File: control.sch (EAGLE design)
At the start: 21 parts, among them IC1 OPA336P, Q1 BSS92, Q2 BSS101

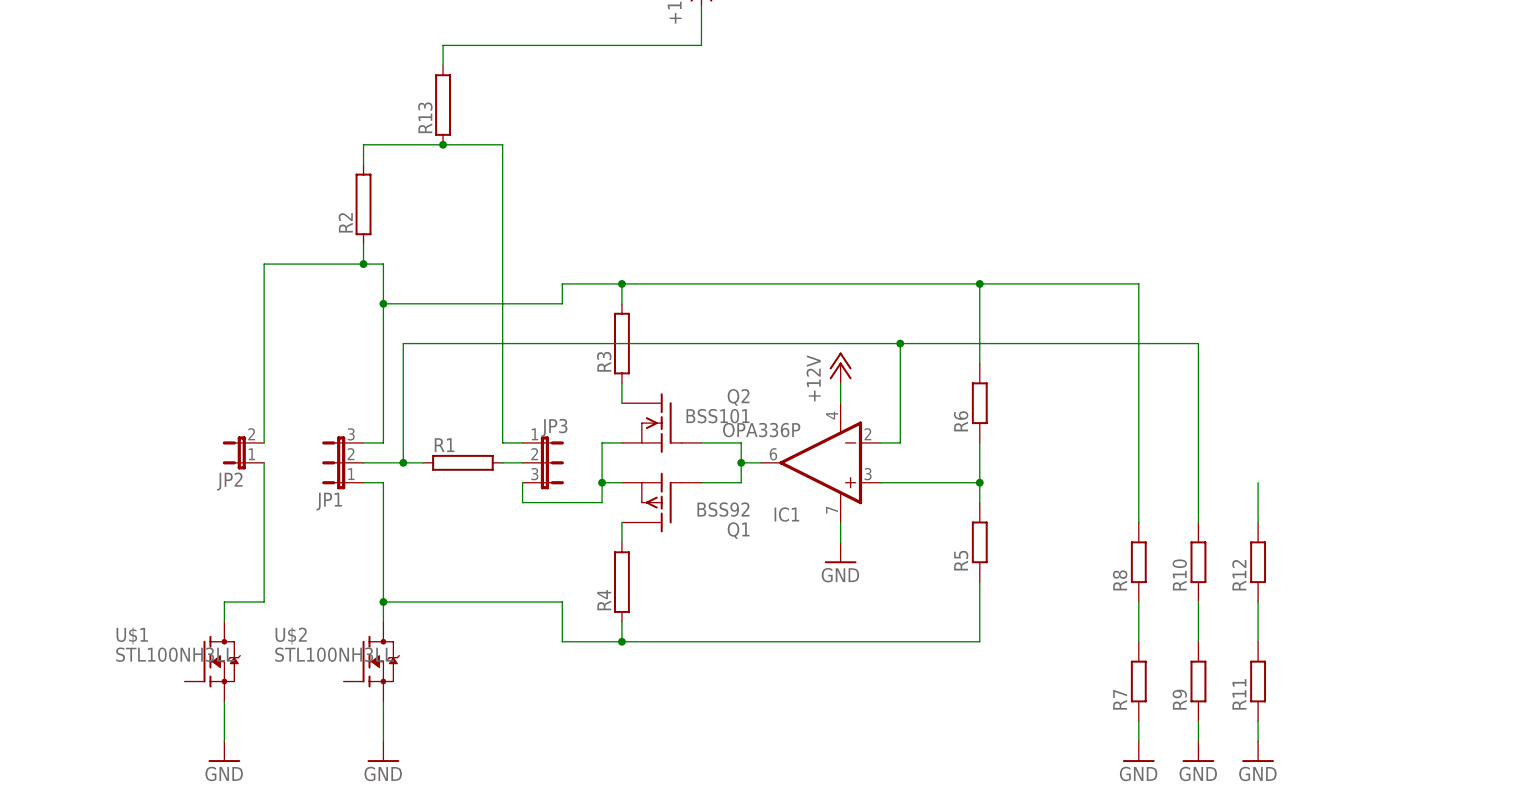
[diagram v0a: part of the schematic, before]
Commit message: +added main discharge path
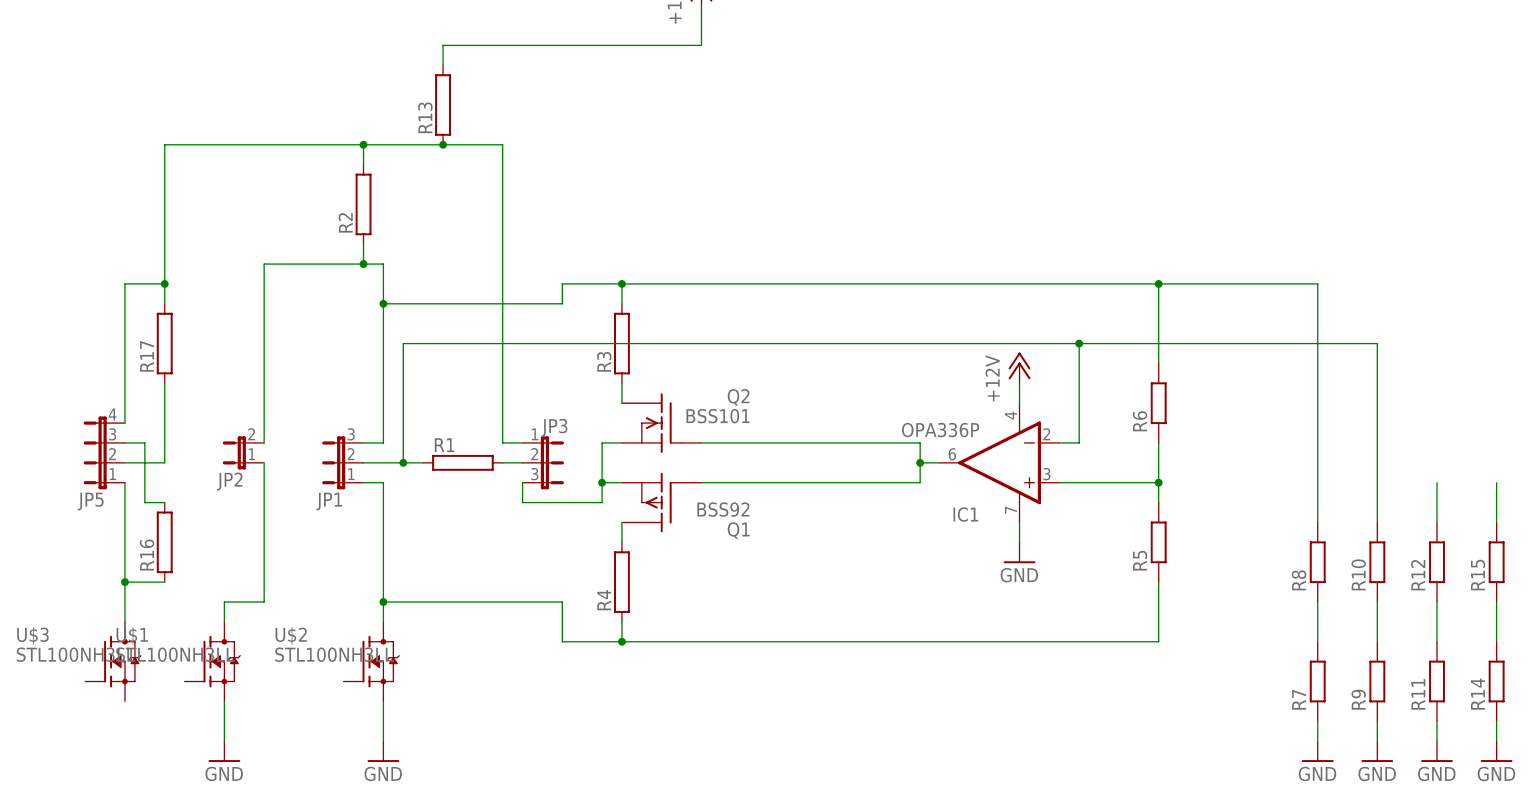
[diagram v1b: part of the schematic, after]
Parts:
- added JP5: (no value), jumper:JP4E
- added R14, R15: (no value), resistor:R-EU_M0805
- added R16, R17: (no value), resistor-power:RRS02M
- added U$3: STL100NH3LL, teile:STL100NH3LL
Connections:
- new net ADC4: JP3.1, JP5.4, R13.1, R15.2, R17.2, R2.2
- new net N$14: JP5.1, R16.1, U$3.D
- new net N$15: JP5.3, R16.2
- new net N$16: JP5.2, R17.1
- net GND: now also R14.1
- net N$10: now also R14.2, R15.1; no longer JP3.1, R13.1, R2.2
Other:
- moved on the sheet: IC1, R10, R11, R12, R5, R6, R7, R8, R9

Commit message: +µC
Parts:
- removed R13: (no value), resistor-power:RRWM5X26
- added C1, C2, C3, C4, C5, C6: (no value), resistor:C-EUC0805K
- added IC2: XMEGA16A4A, atmel:XMEGA16A4A
- added IC3: LM317MBSTT3, v-reg:LM317MBSTT3
- added JP4, JP6: (no value), jumper:JP4E
- added R18, R19, R20: (no value), resistor:R-EU_M0805
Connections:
- new net +3V3: C1.1, C2.1, C3.1, C4.1, C5.1, IC2.AVCC, IC2.VCC, IC2.VCC1, IC2.VCC2, IC3.OUT, R18.2, R20.2
- new net N$17: IC2.!RESET!/PDI_CLK, R18.1
- new net N$18: IC2.PA0, JP6.4
- new net N$19: IC2.PA1, JP6.3
- new net N$20: IC2.PA2, JP6.2
- new net N$21: IC2.PA3, JP6.1
- new net N$22: IC2.PA4, JP4.4
- new net N$23: IC2.PA5, JP4.3
- new net N$24: IC2.PA6, JP4.2
- new net N$25: IC2.PA7, JP4.1
- new net N$27: IC3.ADJ, R19.2, R20.1
- net +12V: now also C6.1, IC3.IN; no longer R13.2
- net ADC4: no longer R13.1
- net GND: now also C1.2, C2.2, C3.2, C4.2, C5.2, C6.2, IC2.GND, IC2.GND1, IC2.GND2, IC2.GND3, R19.1

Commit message: +spannungsregler
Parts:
- added C7, C8: (no value), resistor:C-EUC0805K
- added IC4: OPA336P, burr-brown:OPA336P
- added Q5: TIP41C, transistor-power:TIP41C
- added Q6: TIP42C, transistor-power:TIP42C
- added Q7: BC338, transistor-npn:BC338
- added R13, R21, R22: (no value), resistor:R-EU_M0805
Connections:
- new net N$12: C7.1, Q5.E, R22.1
- new net N$13: Q7.C, R13.2
- new net N$26: Q6.B, R13.1
- new net N$28: C8.1, IC4.OUT, Q7.B
- new net N$30: C8.2, IC4.-IN, R21.1, R22.2
- new net N$31: IC2.PB0, IC4.+IN
- new net N$32: Q5.B, Q6.C
- net +12V: now also IC4.V-, Q5.C, Q6.E
- net GND: now also C7.2, IC4.V+, Q7.E, R21.2
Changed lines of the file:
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@@
 <part name="JP4" library="jumper" deviceset="JP4E" device=""/>
 <part name="JP6" library="jumper" deviceset="JP4E" device=""/>
+<part name="R13" library="resistor" deviceset="R-EU_" device="M0805"/>
+<part name="IC4" library="burr-brown" deviceset="OPA336" device="P"/>
+<part name="R21" library="resistor" deviceset="R-EU_" device="M0805"/>
+<part name="R22" library="resistor" deviceset="R-EU_" device="M0805"/>
+<part name="C7" library="resistor" deviceset="C-EU" device="C0805K"/>
+<part name="C8" library="resistor" deviceset="C-EU" device="C0805K"/>
+<part name="GND13" library="supply1" deviceset="GND" device=""/>
+<part name="GND14" library="supply1" deviceset="GND" device=""/>
+<part name="GND15" library="supply1" deviceset="GND" device=""/>
+<part name="GND16" library="supply1" deviceset="GND" device=""/>
+<part name="Q5" library="transistor-power" deviceset="TIP41C" device=""/>
+<part name="Q6" library="transistor-power" deviceset="TIP42C" device=""/>
+<part name="Q7" library="transistor-npn" deviceset="BC338*" device=""/>
 </parts>
 <sheets>
@@
 <instance part="GND2" gate="1" x="33.02" y="15.24"/>
 <instance part="GND3" gate="1" x="114.3" y="40.64"/>
-<instance part="P+1" gate="1" x="73.66" y="114.3"/>
+<instance part="P+1" gate="1" x="-7.62" y="165.1"/>
 <instance part="P+2" gate="1" x="114.3" y="66.04"/>
 <instance part="R7" gate="G$1" x="152.4" y="25.4" rot="R90"/>
@@
 <instance part="JP4" gate="G$1" x="170.18" y="233.68" rot="R270"/>
 <instance part="JP6" gate="G$1" x="170.18" y="223.52" rot="R270"/>
+<instance part="R13" gate="G$1" x="7.62" y="137.16" rot="R270"/>
+<instance part="IC4" gate="G$1" x="25.4" y="121.92" rot="R180"/>
+<instance part="R21" gate="G$1" x="45.72" y="119.38" rot="R270"/>
+<instance part="R22" gate="G$1" x="45.72" y="134.62" rot="R270"/>
+<instance part="C7" gate="G$1" x="63.5" y="129.54"/>
+<instance part="C8" gate="G$1" x="25.4" y="132.08" rot="R90"/>
+<instance part="GND13" gate="1" x="45.72" y="109.22"/>
+<instance part="GND14" gate="1" x="27.94" y="109.22"/>
+<instance part="GND15" gate="1" x="7.62" y="109.22"/>
+<instance part="GND16" gate="1" x="63.5" y="109.22"/>
+<instance part="Q5" gate="1" x="17.78" y="157.48" rot="R90"/>
+<instance part="Q6" gate="1" x="12.7" y="152.4" rot="R90"/>
+<instance part="Q7" gate="G$1" x="10.16" y="121.92" rot="MR0"/>
 </instances>
 <busses>
@@
 <wire x1="25.4" y1="236.22" x2="25.4" y2="243.84" width="0.1524" layer="91"/>
 </segment>
+<segment>
+<pinref part="IC4" gate="G$1" pin="V+"/>
+<pinref part="GND14" gate="1" pin="GND"/>
+<wire x1="27.94" y1="114.3" x2="27.94" y2="111.76" width="0.1524" layer="91"/>
+</segment>
+<segment>
+<pinref part="R21" gate="G$1" pin="2"/>
+<pinref part="GND13" gate="1" pin="GND"/>
+<wire x1="45.72" y1="114.3" x2="45.72" y2="111.76" width="0.1524" layer="91"/>
+</segment>
+<segment>
+<pinref part="GND16" gate="1" pin="GND"/>
+<pinref part="C7" gate="G$1" pin="2"/>
+<wire x1="63.5" y1="111.76" x2="63.5" y2="124.46" width="0.1524" layer="91"/>
+</segment>
+<segment>
+<pinref part="Q7" gate="G$1" pin="E"/>
+<pinref part="GND15" gate="1" pin="GND"/>
+<wire x1="7.62" y1="111.76" x2="7.62" y2="116.84" width="0.1524" layer="91"/>
+</segment>
 </net>
 <net name="+12V" class="0">
@@
 <pinref part="P+2" gate="1" pin="+12V"/>
 <wire x1="114.3" y1="60.96" x2="114.3" y2="63.5" width="0.1524" layer="91"/>
-</segment>
-<segment>
-<pinref part="P+1" gate="1" pin="+12V"/>
-<wire x1="73.66" y1="111.76" x2="73.66" y2="106.68" width="0.1524" layer="91"/>
-<wire x1="73.66" y1="106.68" x2="40.64" y2="106.68" width="0.1524" layer="91"/>
-<wire x1="40.64" y1="106.68" x2="40.64" y2="104.14" width="0.1524" layer="91"/>
 </segment>
 <segment>
@@
 <wire x1="25.4" y1="256.54" x2="25.4" y2="264.16" width="0.1524" layer="91"/>
 <junction x="25.4" y="256.54"/>
+</segment>
+<segment>
+<pinref part="P+1" gate="1" pin="+12V"/>
+<wire x1="-7.62" y1="160.02" x2="-7.62" y2="162.56" width="0.1524" layer="91"/>
+<wire x1="-7.62" y1="160.02" x2="-7.62" y2="129.54" width="0.1524" layer="91"/>
+<pinref part="IC4" gate="G$1" pin="V-"/>
+<wire x1="27.94" y1="129.54" x2="-7.62" y2="129.54" width="0.1524" layer="91"/>
+<pinref part="Q5" gate="1" pin="C"/>
+<wire x1="12.7" y1="160.02" x2="5.08" y2="160.02" width="0.1524" layer="91"/>
+<wire x1="5.08" y1="160.02" x2="5.08" y2="154.94" width="0.1524" layer="91"/>
+<pinref part="Q6" gate="1" pin="E"/>
+<wire x1="5.08" y1="154.94" x2="7.62" y2="154.94" width="0.1524" layer="91"/>
+<wire x1="5.08" y1="160.02" x2="-7.62" y2="160.02" width="0.1524" layer="91"/>
+<junction x="5.08" y="160.02"/>
 </segment>
 </net>
@@
 </segment>
 </net>
+<net name="N$12" class="0">
+<segment>
+<pinref part="C7" gate="G$1" pin="1"/>
+<wire x1="45.72" y1="144.78" x2="63.5" y2="144.78" width="0.1524" layer="91"/>
+<wire x1="63.5" y1="144.78" x2="63.5" y2="132.08" width="0.1524" layer="91"/>
+<pinref part="R22" gate="G$1" pin="1"/>
+<wire x1="45.72" y1="139.7" x2="45.72" y2="144.78" width="0.1524" layer="91"/>
+<pinref part="Q5" gate="1" pin="E"/>
+<wire x1="22.86" y1="160.02" x2="45.72" y2="160.02" width="0.1524" layer="91"/>
+<wire x1="45.72" y1="160.02" x2="45.72" y2="144.78" width="0.1524" layer="91"/>
+<junction x="45.72" y="144.78"/>
+</segment>
+</net>
+<net name="N$28" class="0">
+<segment>
+<pinref part="IC4" gate="G$1" pin="OUT"/>
+<wire x1="17.78" y1="121.92" x2="15.24" y2="121.92" width="0.1524" layer="91"/>
+<wire x1="15.24" y1="121.92" x2="12.7" y2="121.92" width="0.1524" layer="91"/>
+<wire x1="15.24" y1="121.92" x2="15.24" y2="132.08" width="0.1524" layer="91"/>
+<junction x="15.24" y="121.92"/>
+<pinref part="C8" gate="G$1" pin="1"/>
+<wire x1="15.24" y1="132.08" x2="22.86" y2="132.08" width="0.1524" layer="91"/>
+<pinref part="Q7" gate="G$1" pin="B"/>
+</segment>
+</net>
+<net name="N$30" class="0">
+<segment>
+<pinref part="IC4" gate="G$1" pin="-IN"/>
+<wire x1="33.02" y1="124.46" x2="35.56" y2="124.46" width="0.1524" layer="91"/>
+<wire x1="35.56" y1="124.46" x2="35.56" y2="127" width="0.1524" layer="91"/>
+<pinref part="C8" gate="G$1" pin="2"/>
+<wire x1="35.56" y1="127" x2="35.56" y2="132.08" width="0.1524" layer="91"/>
+<wire x1="35.56" y1="132.08" x2="30.48" y2="132.08" width="0.1524" layer="91"/>
+<pinref part="R22" gate="G$1" pin="2"/>
+<pinref part="R21" gate="G$1" pin="1"/>
+<wire x1="45.72" y1="129.54" x2="45.72" y2="127" width="0.1524" layer="91"/>
+<wire x1="45.72" y1="127" x2="45.72" y2="124.46" width="0.1524" layer="91"/>
+<wire x1="35.56" y1="127" x2="45.72" y2="127" width="0.1524" layer="91"/>
+<junction x="35.56" y="127"/>
+<junction x="45.72" y="127"/>
+</segment>
+</net>
+<net name="N$31" class="0">
+<segment>
+<pinref part="IC2" gate="G$1" pin="PB0"/>
+<wire x1="157.48" y1="205.74" x2="172.72" y2="205.74" width="0.1524" layer="91"/>
+<wire x1="172.72" y1="205.74" x2="172.72" y2="121.92" width="0.1524" layer="91"/>
+<pinref part="IC4" gate="G$1" pin="+IN"/>
+<wire x1="172.72" y1="121.92" x2="33.02" y2="121.92" width="0.1524" layer="91"/>
+<wire x1="33.02" y1="121.92" x2="33.02" y2="119.38" width="0.1524" layer="91"/>
+</segment>
+</net>
+<net name="N$32" class="0">
+<segment>
+<pinref part="Q5" gate="1" pin="B"/>
+<pinref part="Q6" gate="1" pin="C"/>
+</segment>
+</net>
+<net name="N$13" class="0">
+<segment>
+<pinref part="Q7" gate="G$1" pin="C"/>
+<pinref part="R13" gate="G$1" pin="2"/>
+<wire x1="7.62" y1="132.08" x2="7.62" y2="127" width="0.1524" layer="91"/>
+</segment>
+</net>
+<net name="N$26" class="0">
+<segment>
+<pinref part="R13" gate="G$1" pin="1"/>
+<wire x1="7.62" y1="142.24" x2="7.62" y2="144.78" width="0.1524" layer="91"/>
+<pinref part="Q6" gate="1" pin="B"/>
+<wire x1="7.62" y1="144.78" x2="12.7" y2="144.78" width="0.1524" layer="91"/>
+<wire x1="12.7" y1="144.78" x2="12.7" y2="149.86" width="0.1524" layer="91"/>
+</segment>
+</net>

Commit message: shrinking
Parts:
- added Q3: BC548, transistor-npn:BC548
- added Q4: BC557C, transistor-pnp:BC557C
- added Q8: BSS123, transistor-small-signal:BSS123
- added R23, R24, R25, R26, R27, R28, R29, R30: (no value), resistor:R-EU_0207/2V
- added R31: (no value), resistor:R-EU_M0805
- C7: value (none) -> 100n
- C8: value (none) -> 100p
- Q1: value BSS92 -> BSS123; device transistor-fet:BSS92 -> transistor-small-signal:BSS123
- Q2: value BSS101 -> BSS123; device transistor-fet:BSS101 -> transistor-small-signal:BSS123
- R1, R2: device resistor-power:RRS02M -> resistor:R-EU_M0805
- R16, R17: value (none) -> 4R7; device resistor-power:RRS02M -> resistor-power:RKH208-8R
- R3, R4: value (none) -> 10R; device resistor-power:RRS02M -> resistor-power:RHPS58
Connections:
- new net N$29: R23.2, R28.2, R29.1, R30.1
- new net N$33: R24.1, R25.1, R26.2, R27.2
- new net N$34: JP3.3, Q3.E, Q4.E
- new net N$35: Q2.D, R2.1, U$1.G
- new net N$36: Q8.D, R1.1, U$2.G
- net +12V: now also R1.2, R2.2, R31.2
- net ADC1: now also R26.1, R27.1; no longer R2.1
- net ADC2: now also R29.2, R30.2; no longer R1.1
- net ADC3: now also R23.1, R28.1; no longer R1.2
- net ADC4: now also R17.1, R24.2, R25.2; no longer R17.2, R2.2
- net GND: now also Q1.S, Q2.S, Q8.S, U$3.S
- net N$16: now also R17.2; no longer R17.1
- net N$6: now also Q1.D, R31.1, U$3.G; no longer JP3.3, Q1.S, Q2.S
- net N$7: now also Q3.C; no longer Q2.D
- net N$8: now also Q4.C; no longer Q1.D
- net N$9: now also Q3.B, Q4.B; no longer Q1.G, Q2.G
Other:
- moved on the sheet: JP3, R17, R3, R4, U$1, U$2

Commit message: noch falsche layer
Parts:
- removed IC1, IC4: OPA336P, burr-brown:OPA336P
- added C10, C9: (no value), resistor:CPOL-EUE2.5-7
- added IC5: LM358N, linear:LM358N
- added R32, R33, R34, R35, R36, R37, R38, R39, R40, R41, R42, R43, R44, R45, R46, R47, R48: (no value), resistor:R-EU_M0805
- added SV1, SV2: (no value), con-ml:ML66S
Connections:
- removed net N$12: C7.1, Q5.E, R22.1
- new net DIS_A: IC2.PD0, Q1.G
- new net EN_A1: IC2.PD1, Q2.G
- new net EN_A2: IC2.PD2, Q8.G
- new net N$44: IC2.PDI_DATA, SV2.1
- net +12V: now also C9.+, IC5P.V+; no longer IC1.V-, IC4.V-
- net +3V3: now also SV2.2
- net ADC2: now also IC5A.-IN; no longer IC1.-IN
- net ADC4: now also C10.+, C7.1, Q5.E, R22.1, R32.2
- net GND: now also C10.-, C9.-, IC5P.V-, R33.1, R34.1, R35.1, R36.1, R37.1, R38.1, R39.1, R40.1, SV2.6; no longer IC1.V+, IC4.V+
- net N$11: now also IC5A.+IN; no longer IC1.+IN
- net N$17: now also SV2.5
- net N$18: now also R33.2, R41.1
- net N$19: now also R34.2, R42.1
- net N$20: now also R35.2, R43.1
- net N$21: now also R36.2, R44.1
- net N$22: now also R37.2, R45.1
- net N$23: now also R38.2, R46.1
- net N$24: now also R39.2, R47.1
- net N$25: now also R40.2, R48.1
- net N$28: now also IC5B.OUT; no longer IC4.OUT
- net N$30: now also IC5B.-IN; no longer IC4.-IN
- net N$31: now also IC5B.+IN; no longer IC4.+IN
- net N$32: now also R32.1
- net N$9: now also IC5A.OUT; no longer IC1.OUT
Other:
- moved on the sheet: JP1, JP2, JP3, JP4, JP5, JP6, Q1, Q2, Q3, Q4, Q8, R1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

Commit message: layer korrigiert
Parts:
- removed R10, R11, R12, R14, R15, R7, R8, R9: (no value), resistor:R-EU_M0805
- removed SV1: (no value), con-ml:ML66S
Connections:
- removed net N$10: R14.2, R15.1
- removed net N$2: R11.2, R12.1
- removed net N$3: R10.1, R9.2
- removed net N$5: R7.2, R8.1
- net ADC1: no longer R8.2
- net ADC2: no longer R10.2
- net ADC3: no longer R12.2
- net ADC4: no longer R15.2
- net GND: no longer R11.1, R14.1, R7.1, R9.1
